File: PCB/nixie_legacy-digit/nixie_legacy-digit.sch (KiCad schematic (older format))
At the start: 7 parts

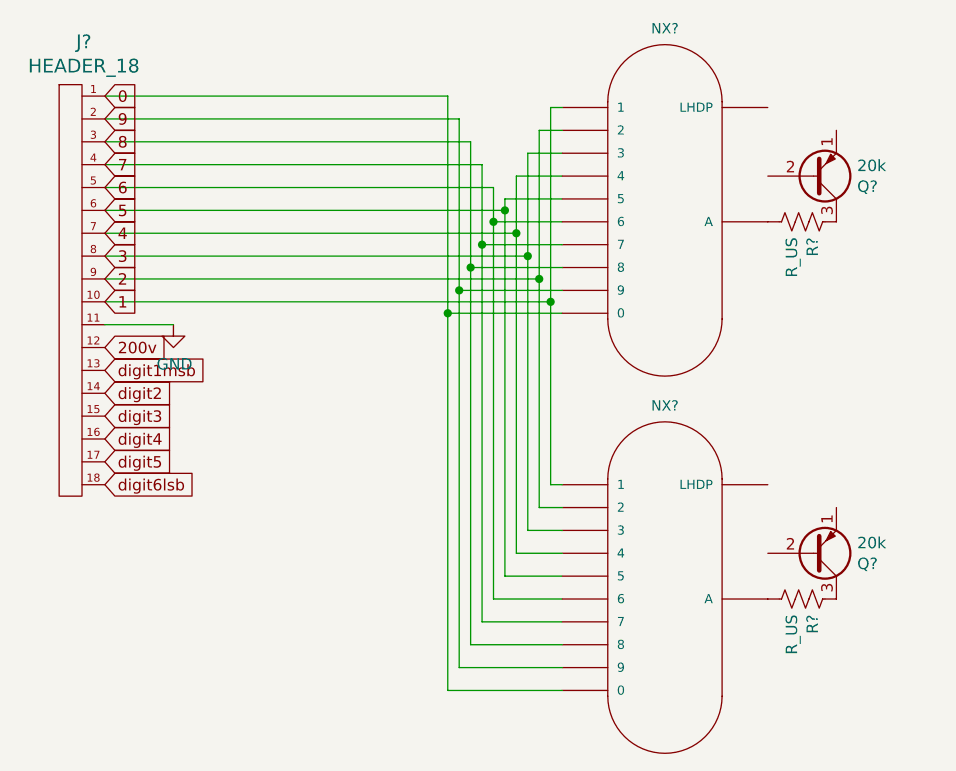
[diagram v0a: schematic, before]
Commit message: digit pcb v1. extra long so that it can fit in my specific clock enclosure. made a "safe to cut" zone so it can be shortened for other applications
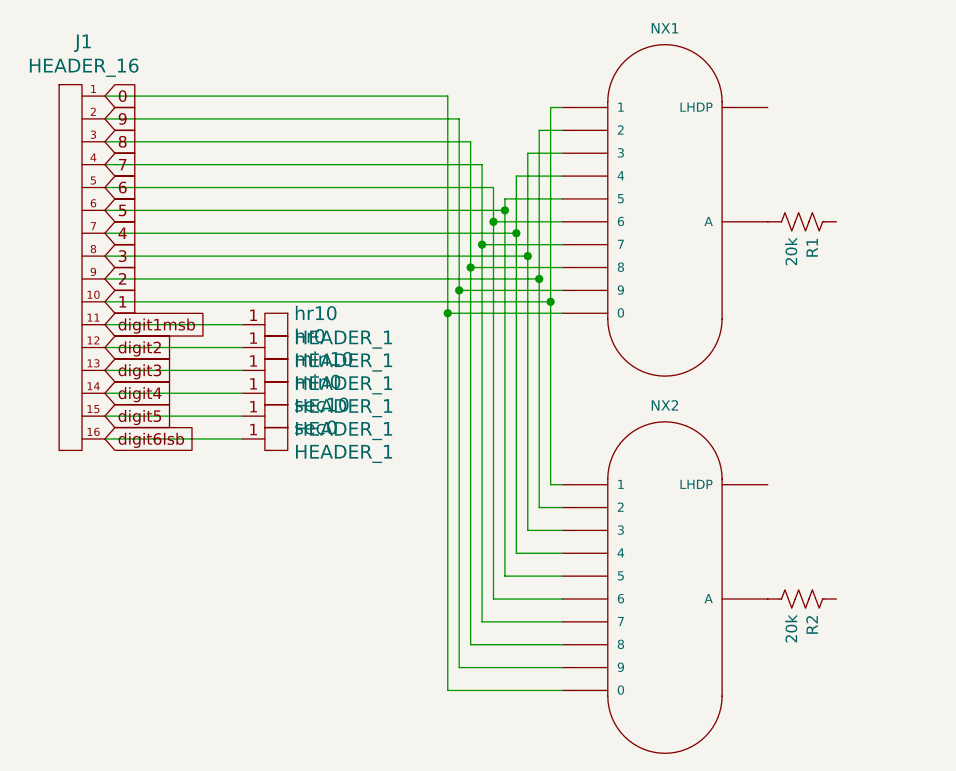
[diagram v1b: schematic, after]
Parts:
- removed J?: HEADER_18, symbol w_connectors:HEADER_18
- removed Q? (x2): 20k, Package_TO_SOT_THT:TO-92_Inline, symbol Transistor_BJT:MPSA92
- added J1: HEADER_16, Connector_PinHeader_2.54mm:PinHeader_2x08_P2.54mm_Vertical, symbol w_connectors:HEADER_16
- added hr0, hr10, min0, min10, sec0, sec10: HEADER_1, customPartsLibrary:Single_pad-1x1, symbol w_connectors:HEADER_1
- NX1, NX2: renamed from NX?; footprint nixies-us_IN-12 -> nixies-us:nixies-us-IN-12-DSUB
- R1, R2: renamed from R?; value R_US -> 20k; footprint (none) -> Resistor_THT:R_Axial_DIN0207_L6.3mm_D2.5mm_P7.62mm_Horizontal
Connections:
- net 0: now also J1.1
- net 1: now also J1.10
- net 2: now also J1.9
- net 3: now also J1.8
- net 4: now also J1.7
- net 5: now also J1.6
- net 6: now also J1.5
- net 7: now also J1.4
- net 8: now also J1.3
- net 9: now also J1.2
- net digit1msb: now also J1.11, hr10.1
- net digit2: now also J1.12, hr0.1
- net digit3: now also J1.13, min10.1
- net digit4: now also J1.14, min0.1
- net digit5: now also J1.15, sec10.1
- net digit6lsb: now also J1.16, sec0.1

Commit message: digit pcb updated. added breakout for left decimal point (for 4-digit clocks)
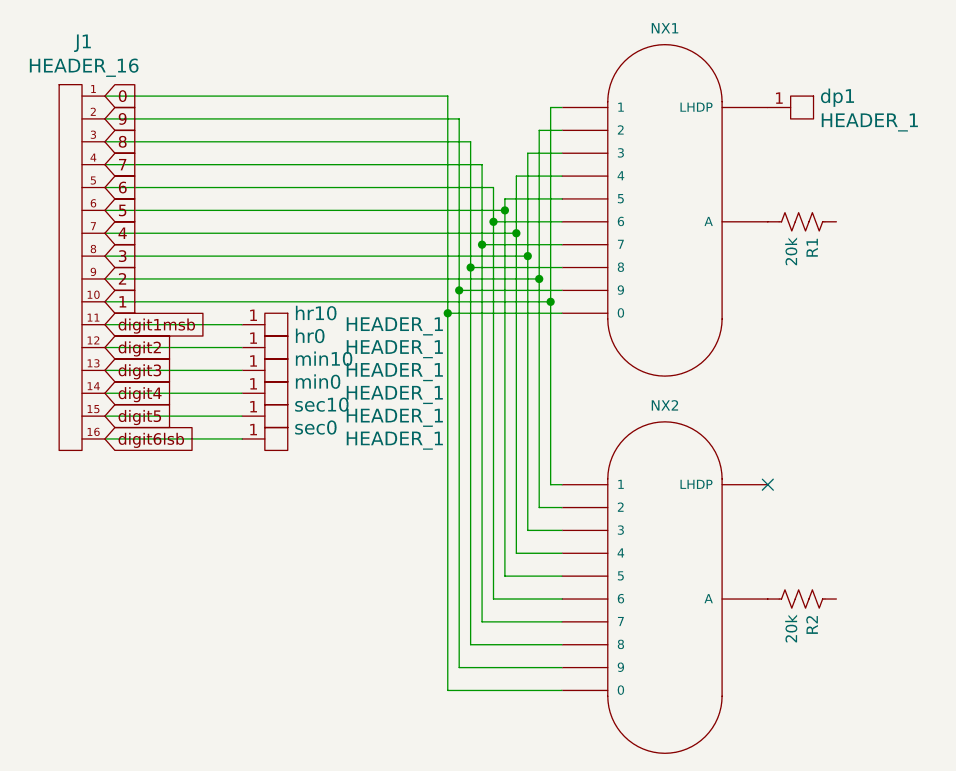
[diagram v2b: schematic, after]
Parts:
- added dp1: HEADER_1, customPartsLibrary:Single_pad-1x1, symbol w_connectors:HEADER_1
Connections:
- net at NX1.LHDP: now also dp1.1
- no-connect marks 0 -> 1
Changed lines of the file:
@@
 P 2300 2250
 F 0 "min10" H 2428 2298 60  0000 L CNN
-F 1 "HEADER_1" H 2428 2192 60  0000 L CNN
+F 1 "HEADER_1" H 2650 2250 60  0000 L CNN
 F 2 "customPartsLibrary:Single_pad-1x1" H 2300 2250 60  0001 C CNN
 F 3 "" H 2300 2250 60  0000 C CNN
@@
 P 2300 2350
 F 0 "min0" H 2428 2398 60  0000 L CNN
-F 1 "HEADER_1" H 2428 2292 60  0000 L CNN
+F 1 "HEADER_1" H 2650 2350 60  0000 L CNN
 F 2 "customPartsLibrary:Single_pad-1x1" H 2300 2350 60  0001 C CNN
 F 3 "" H 2300 2350 60  0000 C CNN
@@
 P 2300 2450
 F 0 "sec10" H 2428 2498 60  0000 L CNN
-F 1 "HEADER_1" H 2428 2392 60  0000 L CNN
+F 1 "HEADER_1" H 2650 2450 60  0000 L CNN
 F 2 "customPartsLibrary:Single_pad-1x1" H 2300 2450 60  0001 C CNN
 F 3 "" H 2300 2450 60  0000 C CNN
@@
 P 2300 2550
 F 0 "sec0" H 2428 2598 60  0000 L CNN
-F 1 "HEADER_1" H 2428 2492 60  0000 L CNN
+F 1 "HEADER_1" H 2650 2550 60  0000 L CNN
 F 2 "customPartsLibrary:Single_pad-1x1" H 2300 2550 60  0001 C CNN
 F 3 "" H 2300 2550 60  0000 C CNN
@@
 P 2300 2050
 F 0 "hr10" H 2428 2098 60  0000 L CNN
-F 1 "HEADER_1" H 2428 1992 60  0000 L CNN
+F 1 "HEADER_1" H 2650 2050 60  0000 L CNN
 F 2 "customPartsLibrary:Single_pad-1x1" H 2300 2050 60  0001 C CNN
 F 3 "" H 2300 2050 60  0000 C CNN
@@
 P 2300 2150
 F 0 "hr0" H 2428 2198 60  0000 L CNN
-F 1 "HEADER_1" H 2428 2092 60  0000 L CNN
+F 1 "HEADER_1" H 2650 2150 60  0000 L CNN
 F 2 "customPartsLibrary:Single_pad-1x1" H 2300 2150 60  0001 C CNN
 F 3 "" H 2300 2150 60  0000 C CNN
@@
 Wire Wire Line
 	2200 2550 1600 2550
+$Comp
+L w_connectors:HEADER_1 dp1
+U 1 1 61696992
+P 4600 1100
+F 0 "dp1" H 4728 1148 60  0000 L CNN
+F 1 "HEADER_1" H 4728 1042 60  0000 L CNN
+F 2 "customPartsLibrary:Single_pad-1x1" H 4600 1100 60  0001 C CNN
+F 3 "" H 4600 1100 60  0000 C CNN
+	1    4600 1100
+	1    0    0    -1
+$EndComp
+NoConn ~ 4500 2750
 $EndSCHEMATC

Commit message: -power board: updated 7805 footprint to better fit piece, "A55" instead of "A56", 9v input pad shape swap so that ground makes sense -digit board: added resistor value, vertical connector, correct pinout for rear mounting to match header population on demux board -new_rtc_pcbHack: deprecated. works with v1 of digit boards (with bad header pinout) but no longer needed. did not update with time demux, only displayed idle animation and set menu
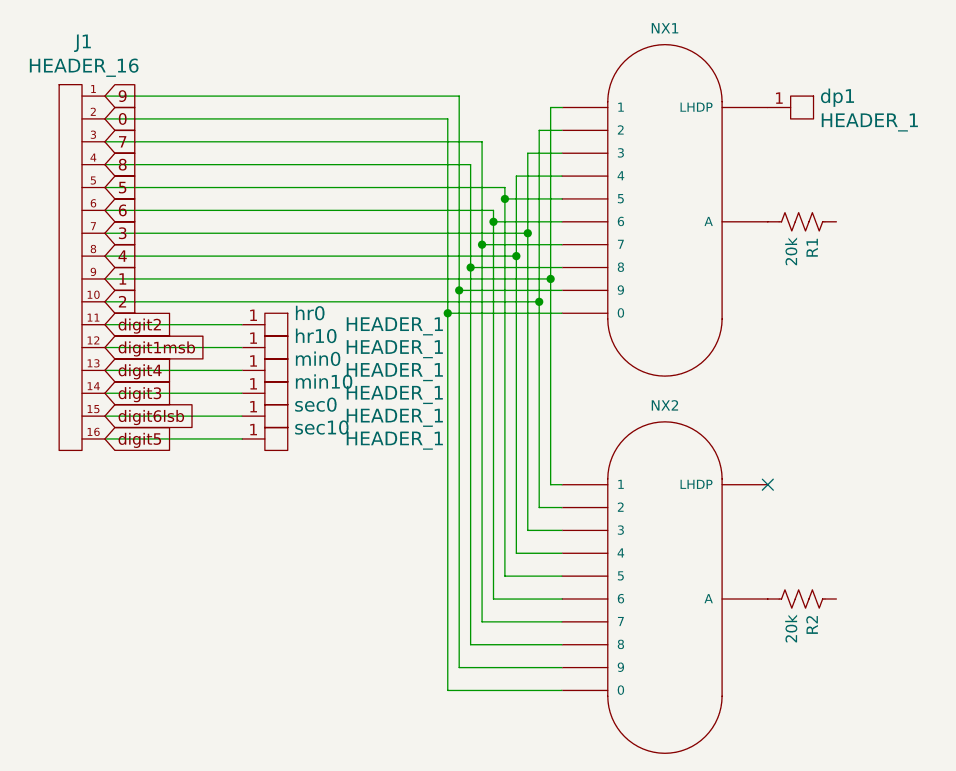
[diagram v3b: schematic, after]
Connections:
- net 0: now also J1.2; no longer J1.1
- net 1: now also J1.9; no longer J1.10
- net 2: now also J1.10; no longer J1.9
- net 3: now also J1.7; no longer J1.8
- net 4: now also J1.8; no longer J1.7
- net 5: now also J1.5; no longer J1.6
- net 6: now also J1.6; no longer J1.5
- net 7: now also J1.3; no longer J1.4
- net 8: now also J1.4; no longer J1.3
- net 9: now also J1.1; no longer J1.2
- net digit1msb: now also J1.12; no longer J1.11
- net digit2: now also J1.11; no longer J1.12
- net digit3: now also J1.14; no longer J1.13
- net digit4: now also J1.13; no longer J1.14
- net digit5: now also J1.16; no longer J1.15
- net digit6lsb: now also J1.15; no longer J1.16
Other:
- moved on the sheet: hr0, hr10, min0, min10, sec0, sec10
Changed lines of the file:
@@
 	1    0    0    -1
 $EndComp
+Text GLabel 1600 1150 2    50   Input ~ 0
+0
 Text GLabel 1600 1050 2    50   Input ~ 0
-0
-Text GLabel 1600 1150 2    50   Input ~ 0
 9
+Text GLabel 1600 1350 2    50   Input ~ 0
+8
 Text GLabel 1600 1250 2    50   Input ~ 0
-8
-Text GLabel 1600 1350 2    50   Input ~ 0
 7
+Text GLabel 1600 1550 2    50   Input ~ 0
+6
 Text GLabel 1600 1450 2    50   Input ~ 0
-6
-Text GLabel 1600 1550 2    50   Input ~ 0
 5
+Text GLabel 1600 1750 2    50   Input ~ 0
+4
 Text GLabel 1600 1650 2    50   Input ~ 0
-4
-Text GLabel 1600 1750 2    50   Input ~ 0
 3
+Text GLabel 1600 1950 2    50   Input ~ 0
+2
 Text GLabel 1600 1850 2    50   Input ~ 0
-2
-Text GLabel 1600 1950 2    50   Input ~ 0
 1
+Text GLabel 1600 2150 2    50   Input ~ 0
+digit1msb
 Text GLabel 1600 2050 2    50   Input ~ 0
-digit1msb
-Text GLabel 1600 2150 2    50   Input ~ 0
 digit2
+Text GLabel 1600 2350 2    50   Input ~ 0
+digit3
 Text GLabel 1600 2250 2    50   Input ~ 0
-digit3
-Text GLabel 1600 2350 2    50   Input ~ 0
 digit4
+Text GLabel 1600 2550 2    50   Input ~ 0
+digit5
 Text GLabel 1600 2450 2    50   Input ~ 0
-digit5
-Text GLabel 1600 2550 2    50   Input ~ 0
 digit6lsb
 $Comp
@@
 	3600 1200 3500 1200
 Wire Wire Line
-	3500 1200 3500 1850
-Wire Wire Line
 	3500 2850 3600 2850
 Wire Wire Line
@@
 	3600 1400 3400 1400
 Wire Wire Line
-	3400 1400 3400 1650
-Wire Wire Line
 	3400 3050 3600 3050
 Wire Wire Line
@@
 	3100 3650 3600 3650
 Wire Wire Line
-	1600 1950 3550 1950
-Wire Wire Line
-	3550 1950 3550 1100
-Wire Wire Line
-	1600 1850 3500 1850
-Wire Wire Line
-	1600 1750 3450 1750
-Wire Wire Line
-	3450 1750 3450 1300
-Wire Wire Line
-	1600 1650 3400 1650
-Wire Wire Line
-	1600 1550 3350 1550
-Wire Wire Line
-	3350 1550 3350 1500
-Wire Wire Line
-	3300 1450 3300 1600
-Wire Wire Line
-	1600 1450 3300 1450
-Wire Wire Line
-	3250 1350 3250 1700
-Wire Wire Line
-	1600 1350 3250 1350
-Wire Wire Line
-	3200 1250 3200 1800
-Wire Wire Line
-	1600 1250 3200 1250
-Wire Wire Line
-	3150 1150 3150 1900
-Wire Wire Line
-	1600 1150 3150 1150
-Wire Wire Line
-	3100 1050 1600 1050
-Connection ~ 3400 1650
-Wire Wire Line
-	3400 1650 3400 3050
-Connection ~ 3500 1850
-Wire Wire Line
-	3500 1850 3500 2850
-Wire Wire Line
-	3100 2000 3100 1050
+	1600 1850 3550 1850
+Wire Wire Line
+	1600 1950 3500 1950
+Wire Wire Line
+	1600 1650 3450 1650
+Wire Wire Line
+	1600 1750 3400 1750
+Wire Wire Line
+	1600 1550 3300 1550
+Wire Wire Line
+	1600 1350 3200 1350
 Wire Wire Line
 	3100 2000 3100 3650
@@
 Wire Wire Line
 	3300 1600 3300 3250
-Connection ~ 3350 1550
-Wire Wire Line
-	3350 3150 3350 1550
-Connection ~ 3450 1750
-Wire Wire Line
-	3450 2950 3450 1750
-Connection ~ 3550 1950
-Wire Wire Line
-	3550 2750 3550 1950
 $Comp
 L nixies-us:IN-12BORIGINAL NX1
@@
 L w_connectors:HEADER_1 min10
 U 1 1 616638CE
+P 2300 2350
+F 0 "min10" H 2428 2398 60  0000 L CNN
+F 1 "HEADER_1" H 2650 2350 60  0000 L CNN
+F 2 "customPartsLibrary:Single_pad-1x1" H 2300 2350 60  0001 C CNN
+F 3 "" H 2300 2350 60  0000 C CNN
+	1    2300 2350
+	1    0    0    -1
+$EndComp
+$Comp
+L w_connectors:HEADER_1 min0
+U 1 1 61666A78
 P 2300 2250
-F 0 "min10" H 2428 2298 60  0000 L CNN
+F 0 "min0" H 2428 2298 60  0000 L CNN
 F 1 "HEADER_1" H 2650 2250 60  0000 L CNN
 F 2 "customPartsLibrary:Single_pad-1x1" H 2300 2250 60  0001 C CNN
@@
 $EndComp
 $Comp
-L w_connectors:HEADER_1 min0
-U 1 1 61666A78
-P 2300 2350
-F 0 "min0" H 2428 2398 60  0000 L CNN
-F 1 "HEADER_1" H 2650 2350 60  0000 L CNN
-F 2 "customPartsLibrary:Single_pad-1x1" H 2300 2350 60  0001 C CNN
-F 3 "" H 2300 2350 60  0000 C CNN
-	1    2300 2350
-	1    0    0    -1
-$EndComp
-$Comp
 L w_connectors:HEADER_1 sec10
 U 1 1 61667A7E
+P 2300 2550
+F 0 "sec10" H 2428 2598 60  0000 L CNN
+F 1 "HEADER_1" H 2650 2550 60  0000 L CNN
+F 2 "customPartsLibrary:Single_pad-1x1" H 2300 2550 60  0001 C CNN
+F 3 "" H 2300 2550 60  0000 C CNN
+	1    2300 2550
+	1    0    0    -1
+$EndComp
+$Comp
+L w_connectors:HEADER_1 sec0
+U 1 1 61667A88
 P 2300 2450
-F 0 "sec10" H 2428 2498 60  0000 L CNN
+F 0 "sec0" H 2428 2498 60  0000 L CNN
 F 1 "HEADER_1" H 2650 2450 60  0000 L CNN
 F 2 "customPartsLibrary:Single_pad-1x1" H 2300 2450 60  0001 C CNN
@@
 $EndComp
 $Comp
-L w_connectors:HEADER_1 sec0
-U 1 1 61667A88
-P 2300 2550
-F 0 "sec0" H 2428 2598 60  0000 L CNN
-F 1 "HEADER_1" H 2650 2550 60  0000 L CNN
-F 2 "customPartsLibrary:Single_pad-1x1" H 2300 2550 60  0001 C CNN
-F 3 "" H 2300 2550 60  0000 C CNN
-	1    2300 2550
-	1    0    0    -1
-$EndComp
-$Comp
 L w_connectors:HEADER_1 hr10
 U 1 1 6166A207
+P 2300 2150
+F 0 "hr10" H 2428 2198 60  0000 L CNN
+F 1 "HEADER_1" H 2650 2150 60  0000 L CNN
+F 2 "customPartsLibrary:Single_pad-1x1" H 2300 2150 60  0001 C CNN
+F 3 "" H 2300 2150 60  0000 C CNN
+	1    2300 2150
+	1    0    0    -1
+$EndComp
+$Comp
+L w_connectors:HEADER_1 hr0
+U 1 1 6166A211
 P 2300 2050
-F 0 "hr10" H 2428 2098 60  0000 L CNN
+F 0 "hr0" H 2428 2098 60  0000 L CNN
 F 1 "HEADER_1" H 2650 2050 60  0000 L CNN
 F 2 "customPartsLibrary:Single_pad-1x1" H 2300 2050 60  0001 C CNN
@@
 	1    0    0    -1
 $EndComp
-$Comp
-L w_connectors:HEADER_1 hr0
-U 1 1 6166A211
-P 2300 2150
-F 0 "hr0" H 2428 2198 60  0000 L CNN
-F 1 "HEADER_1" H 2650 2150 60  0000 L CNN
-F 2 "customPartsLibrary:Single_pad-1x1" H 2300 2150 60  0001 C CNN
-F 3 "" H 2300 2150 60  0000 C CNN
-	1    2300 2150
-	1    0    0    -1
-$EndComp
+Wire Wire Line
+	2200 2150 1600 2150
 Wire Wire Line
 	2200 2050 1600 2050
 Wire Wire Line
-	2200 2150 1600 2150
+	2200 2350 1600 2350
 Wire Wire Line
 	2200 2250 1600 2250
 Wire Wire Line
-	2200 2350 1600 2350
+	2200 2550 1600 2550
 Wire Wire Line
 	2200 2450 1600 2450
-Wire Wire Line
-	2200 2550 1600 2550
 $Comp
 L w_connectors:HEADER_1 dp1
@@
 $EndComp
 NoConn ~ 4500 2750
+Wire Wire Line
+	3100 2000 3100 1150
+Wire Wire Line
+	1600 1050 3150 1050
+Wire Wire Line
+	3100 1150 1600 1150
+Wire Wire Line
+	3150 1050 3150 1900
+Wire Wire Line
+	3350 1500 3350 3150
+Wire Wire Line
+	1600 1450 3350 1450
+Wire Wire Line
+	3350 1450 3350 1500
+Connection ~ 3350 1500
+Wire Wire Line
+	3400 1400 3400 1750
+Connection ~ 3450 1650
+Wire Wire Line
+	3450 1650 3450 1300
+Wire Wire Line
+	3450 1650 3450 2950
+Connection ~ 3400 1750
+Wire Wire Line
+	3400 1750 3400 3050
+Wire Wire Line
+	3500 1200 3500 1950
+Connection ~ 3550 1850
+Wire Wire Line
+	3550 1850 3550 1100
+Wire Wire Line
+	3550 1850 3550 2750
+Connection ~ 3500 1950
+Wire Wire Line
+	3500 1950 3500 2850
+Wire Wire Line
+	1600 1250 3250 1250
+Wire Wire Line
+	3250 1250 3250 1700
+Wire Wire Line
+	3200 1350 3200 1800
+Wire Wire Line
+	3300 1550 3300 1600
 $EndSCHEMATC
